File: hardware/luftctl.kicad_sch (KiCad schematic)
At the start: 39 parts, among them J1 PJ-102A, J2 TTL, M1 PWM Fan, M2 PWM Fan, M3 PWM Fan, M4 PWM Fan, M5 PWM Fan, M6 PWM Fan, U1 ESP32-DEVKITC-32D, U2 R-78E5.0-1.0, U3 SN74HCT245N, U5 DS18B20, U6 DS18B20, U7 DS18B20

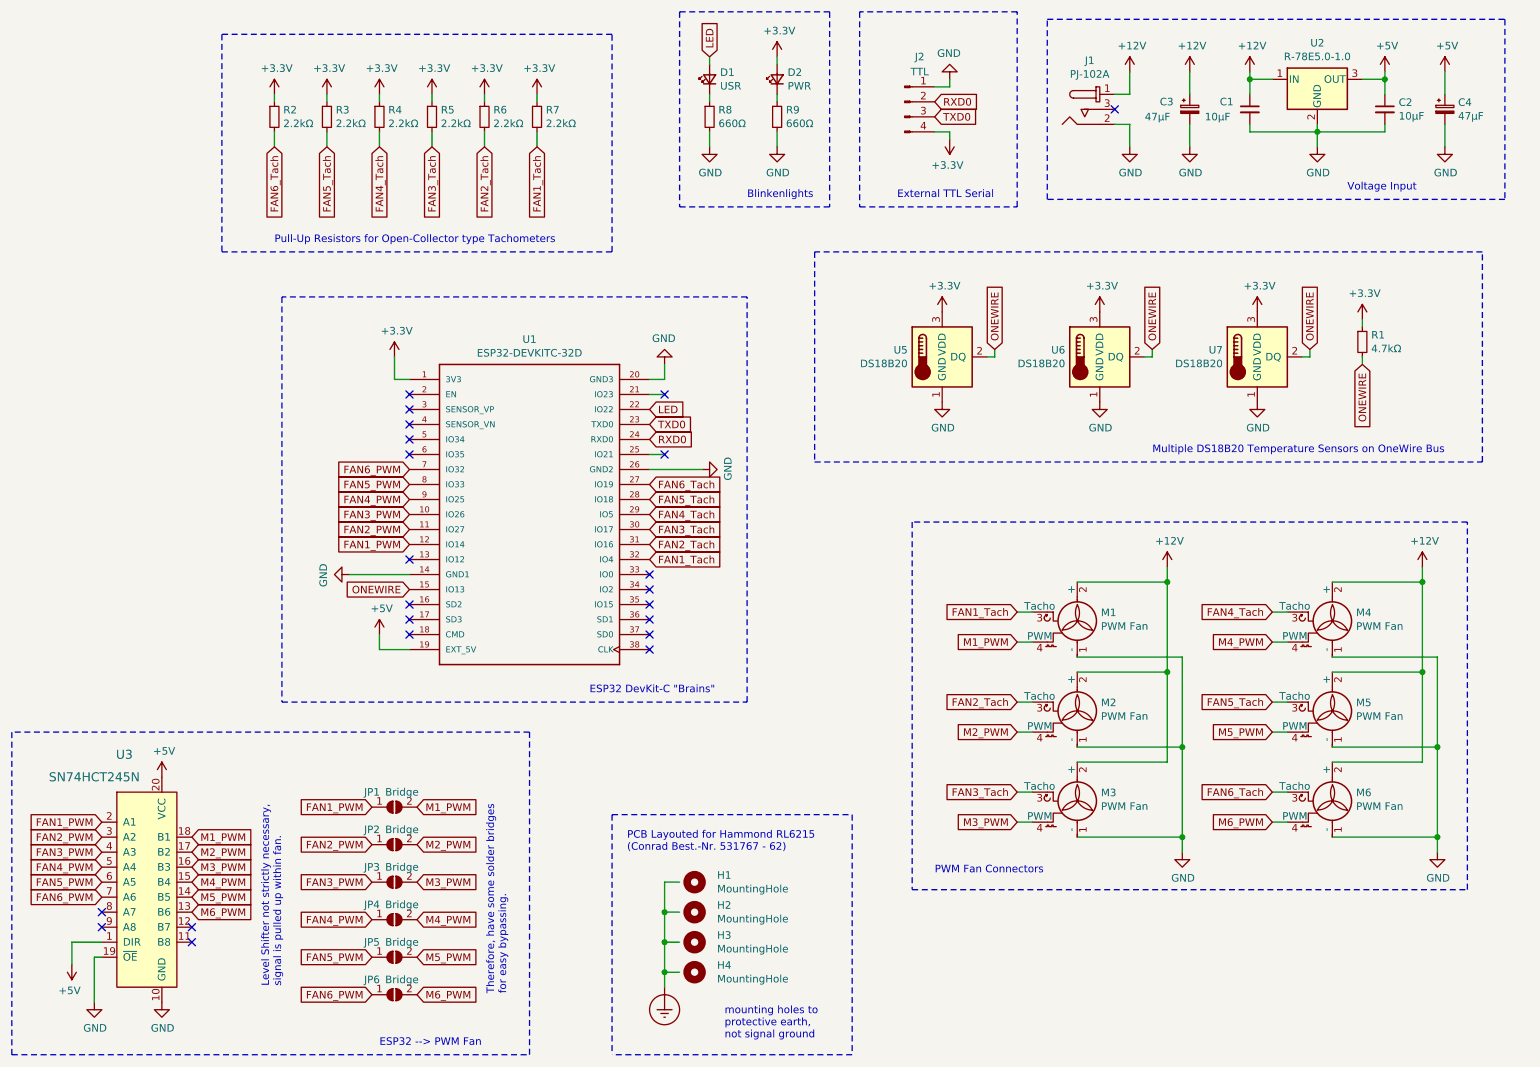
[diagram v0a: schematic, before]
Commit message: redesigned schematic for esp32-c3 module, dummy pcb
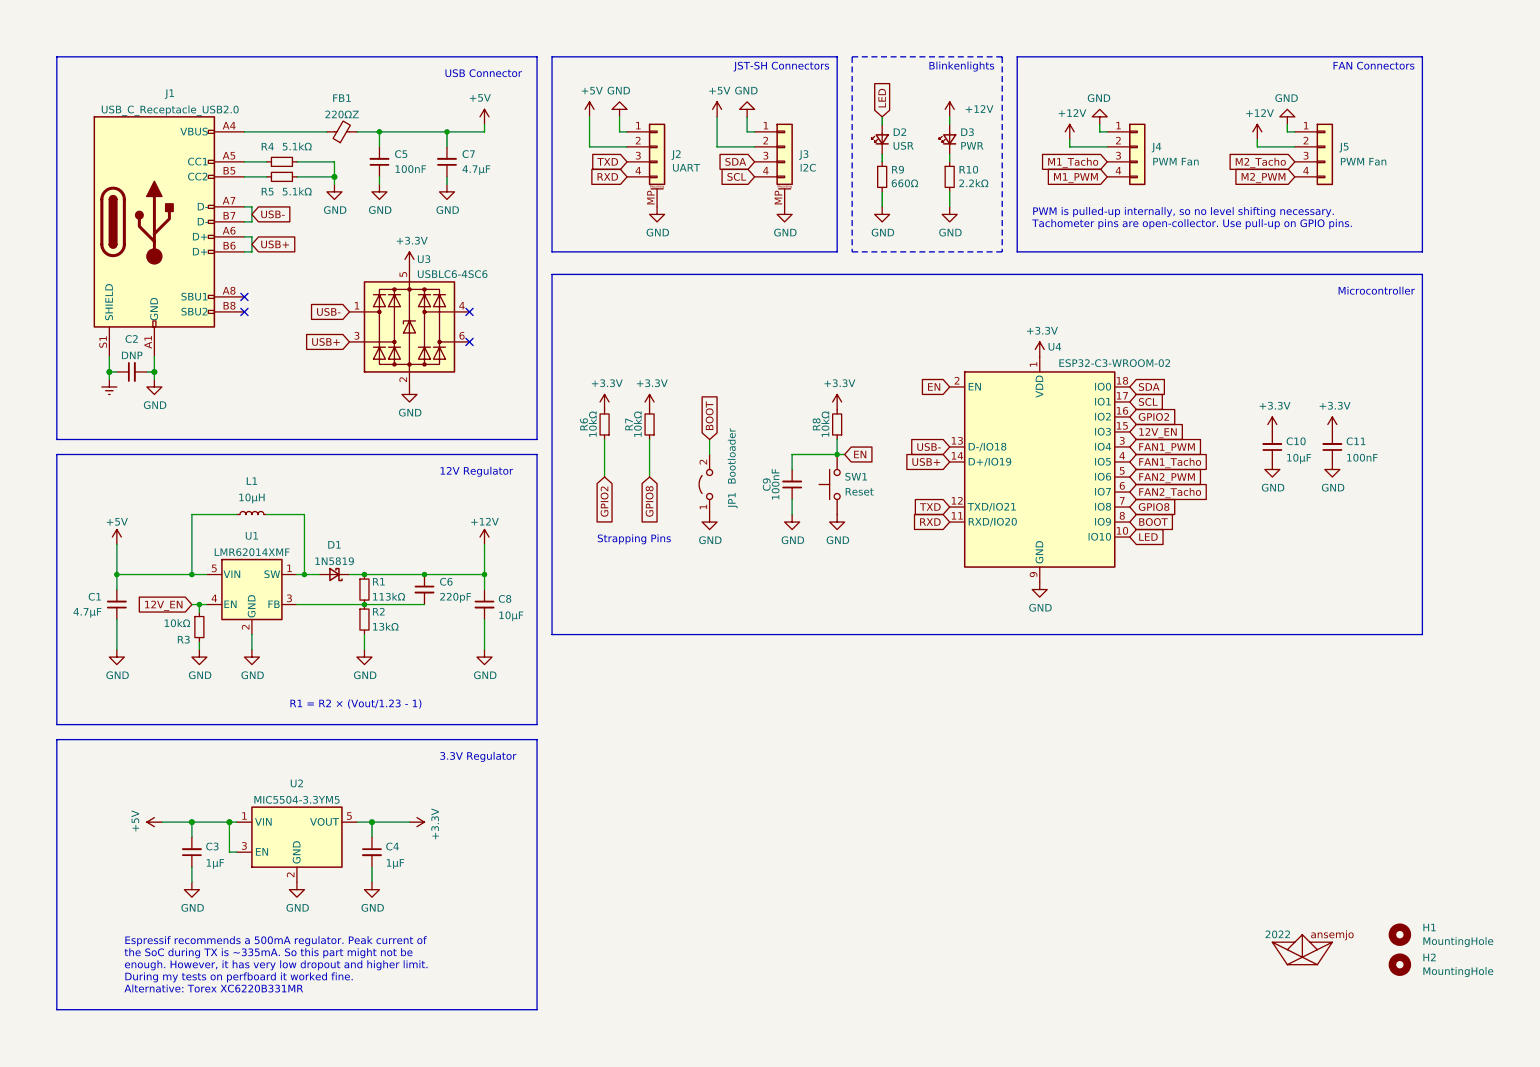
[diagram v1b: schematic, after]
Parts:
- removed C3, C4: 47µF, Capacitor_THT:CP_Radial_D6.3mm_P2.50mm, symbol Device:CP_Small
- removed H3, H4: MountingHole, MountingHole:MountingHole_3.2mm_M3, symbol Mechanical:MountingHole
- removed J1: PJ-102A, digikey-footprints:Barrel_Jack_5.5mmODx2.1mmID_PJ-102A, symbol dk_Barrel-Power-Connectors:PJ-102A
- removed J2: TTL, Connector_PinHeader_2.54mm:PinHeader_1x04_P2.54mm_Vertical, symbol Connector:Conn_01x04_Male
- removed JP1, JP2, JP3, JP4, JP5, JP6: Bridge, Jumper:SolderJumper-2_P1.3mm_Open_TrianglePad1.0x1.5mm, symbol Jumper:SolderJumper_2_Open
- removed M1, M2, M3, M4, M5, M6: PWM Fan, Connector:FanPinHeader_1x04_P2.54mm_Vertical, symbol Motor:Fan_Tacho_PWM
- removed U1: ESP32-DEVKITC-32D, snapeda-lib:MODULE_ESP32-DEVKITC-32D, symbol luftctl-rescue:ESP32-DEVKITC-32D-esp32-devkit
- removed U2: R-78E5.0-1.0, Converter_DCDC:Converter_DCDC_RECOM_R-78E-0.5_THT, symbol Regulator_Switching:R-78E5.0-1.0
- removed U3: SN74HCT245N, Package_DIP:DIP-20_W7.62mm, symbol dk_Logic-Buffers-Drivers-Receivers-Transceivers:SN74LVC245AN
- removed U5, U6, U7: DS18B20, Package_TO_SOT_THT:TO-92_Inline_Wide, symbol Sensor_Temperature:DS18B20
- added A1: 2022, ansemjo:ahoi, symbol ansemjo:ahoi
- added C10, C8: 10µF, Capacitor_SMD:C_0805_2012Metric_Pad1.18x1.45mm_HandSolder, symbol Device:C_Small
- added C11, C5, C9: 100nF, Capacitor_SMD:C_0805_2012Metric_Pad1.18x1.45mm_HandSolder, symbol Device:C_Small
- added C3, C4: 1µF, Capacitor_SMD:C_0805_2012Metric_Pad1.18x1.45mm_HandSolder, symbol Device:C_Small
- added C6: 220pF, Capacitor_SMD:C_0805_2012Metric_Pad1.18x1.45mm_HandSolder, symbol Device:C_Small
- added C7: 4.7µF, Capacitor_SMD:C_0805_2012Metric_Pad1.18x1.45mm_HandSolder, symbol Device:C_Small
- added D1: 1N5819, Diode_SMD:D_SOD-123, symbol Device:D_Schottky_Small
- added FB1: 220ΩZ, Inductor_SMD:L_0805_2012Metric_Pad1.15x1.40mm_HandSolder, symbol Device:Ferrite_Bead_Small
- added J1: USB_C_Receptacle_USB2.0, Connector_USB:USB_C_Receptacle_HRO_TYPE-C-31-M-12, symbol Connector:USB_C_Receptacle_USB2.0
- added J2: UART, Connector_JST:JST_SH_SM04B-SRSS-TB_1x04-1MP_P1.00mm_Horizontal, symbol Connector_Generic_MountingPin:Conn_01x04_MountingPin
- added J3: I2C, Connector_JST:JST_SH_SM04B-SRSS-TB_1x04-1MP_P1.00mm_Horizontal, symbol Connector_Generic_MountingPin:Conn_01x04_MountingPin
- added J4, J5: PWM Fan, Connector:FanPinHeader_1x04_P2.54mm_Vertical, symbol Connector_Generic:Conn_01x04
- added JP1: Bootloader, Button_Switch_SMD:SW_SPST_PTS810, symbol Jumper:Jumper_2_Open
- added L1: 10µH, Inductor_SMD:L_Bourns_SRN6045TA, symbol Device:L_Small
- added R8: 10kΩ, Resistor_SMD:R_0805_2012Metric_Pad1.20x1.40mm_HandSolder, symbol Device:R_Small
- added SW1: Reset, Button_Switch_SMD:SW_SPST_PTS810, symbol Switch:SW_Push
- added U1: LMR62014XMF, Package_TO_SOT_SMD:SOT-23-5, symbol Regulator_Switching:LMR62014XMF
- added U2: MIC5504-3.3YM5, Package_TO_SOT_SMD:SOT-23-5, symbol Regulator_Linear:MIC5504-3.3YM5
- added U3: USBLC6-4SC6, Package_TO_SOT_SMD:SOT-23-6, symbol Power_Protection:USBLC6-4SC6
- added U4: ESP32-C3-WROOM-02, RF_Module:ESP-WROOM-02, symbol local:ESP32-C3-WROOM-02
- C1: value 10µF -> 4.7µF; footprint Capacitor_THT:C_Disc_D5.1mm_W3.2mm_P5.00mm -> Capacitor_SMD:C_0805_2012Metric_Pad1.18x1.45mm_HandSolder
- C2: value 10µF -> DNP; footprint Capacitor_THT:C_Disc_D5.1mm_W3.2mm_P5.00mm -> Capacitor_SMD:C_0805_2012Metric_Pad1.18x1.45mm_HandSolder
- D2: renamed from D1; footprint LED_THT:LED_Rectangular_W5.0mm_H2.0mm -> LED_SMD:LED_0805_2012Metric_Pad1.15x1.40mm_HandSolder
- D3: renamed from D2; footprint LED_THT:LED_Rectangular_W5.0mm_H2.0mm -> LED_SMD:LED_0805_2012Metric_Pad1.15x1.40mm_HandSolder
- H1, H2: footprint MountingHole:MountingHole_3.2mm_M3 -> MountingHole:MountingHole_5.3mm_M5
- R1: value 4.7kΩ -> 113kΩ; footprint Resistor_THT:R_Axial_DIN0207_L6.3mm_D2.5mm_P10.16mm_Horizontal -> Resistor_SMD:R_0805_2012Metric_Pad1.20x1.40mm_HandSolder
- R10: renamed from R9; value 660Ω -> 2.2kΩ; footprint Resistor_THT:R_Axial_DIN0207_L6.3mm_D2.5mm_P10.16mm_Horizontal -> Resistor_SMD:R_0805_2012Metric_Pad1.20x1.40mm_HandSolder
- R2: value 2.2kΩ -> 13kΩ; footprint Resistor_THT:R_Axial_DIN0207_L6.3mm_D2.5mm_P10.16mm_Horizontal -> Resistor_SMD:R_0805_2012Metric_Pad1.20x1.40mm_HandSolder
- R3, R6, R7: value 2.2kΩ -> 10kΩ; footprint Resistor_THT:R_Axial_DIN0207_L6.3mm_D2.5mm_P10.16mm_Horizontal -> Resistor_SMD:R_0805_2012Metric_Pad1.20x1.40mm_HandSolder
- R4, R5: value 2.2kΩ -> 5.1kΩ; footprint Resistor_THT:R_Axial_DIN0207_L6.3mm_D2.5mm_P10.16mm_Horizontal -> Resistor_SMD:R_0805_2012Metric_Pad1.20x1.40mm_HandSolder
- R9: renamed from R8; footprint Resistor_THT:R_Axial_DIN0207_L6.3mm_D2.5mm_P10.16mm_Horizontal -> Resistor_SMD:R_0805_2012Metric_Pad1.20x1.40mm_HandSolder
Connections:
- net FAN1_Tach is gone; now on net +3V3: R7.2
- net FAN2_Tach is gone; now on net +3V3: R6.2
- net FAN4_Tach is gone; now on net GND: R4.2
- net FAN5_Tach is gone; now on net GND: R3.2
- net FAN6_Tach is gone; now on net GND: R2.2
- net +12V: now also D3.2 (A), R1.1, C6.1, C8.1, D1.1 (K), J4.2 (Pin_2), J5.2 (Pin_2); no longer C1.1
- net +3V3: now also C10.2, C11.2, C4.1, R8.2, U2.5 (VOUT), U3.5 (VBUS), U4.1 (VDD); no longer D3.2 (A), R1.1, R2.1, R3.1, R4.1, R5.1, R6.1, R7.1
- net +5V: now also C1.2, C3.2, C5.2, C7.2, FB1.2, J2.2 (Pin_2), J3.2 (Pin_2), L1.1, U1.5 (VIN), U2.1 (VIN), U2.3 (EN); no longer C2.1
- net FAN1_PWM: now also U4.3 (IO4)
- net FAN2_PWM: now also U4.5 (IO6)
- net GND: now also C1.1, R5.1, C10.1, C11.1, C3.1, C4.2, C5.1, C7.1, C8.2, C9.1, J1.A1 (GND), J1.A12 (GND), J1.B1 (GND), J1.B12 (GND), J2.1 (Pin_1), J2.MP (MountPin), J3.1 (Pin_1), J3.MP (MountPin), J4.1 (Pin_1), J5.1 (Pin_1), JP1.1 (A), SW1.1, U1.2 (GND), U2.2 (GND), U3.2 (GND), U4.19 (GND), U4.9 (GND); no longer C1.2
- net LED: now also U4.10 (IO10)
- net M1_PWM: now also J4.4 (Pin_4)
- net M2_PWM: now also J5.4 (Pin_4)
- net FAN3_Tach: no longer names the net of R5.2
- net FAN3_Tach: now also J1.B5 (CC2)
- net ONEWIRE: no longer names the net of R1.2
- net ONEWIRE: now also R2.1, C6.2, U1.3 (FB)
- new net: J1.A5 (CC1), R4.1
- new net: FB1.1, J1.A4 (VBUS), J1.A9 (VBUS), J1.B4 (VBUS), J1.B9 (VBUS)
- new net: D1.2 (A), L1.2, U1.1 (SW)
- new net 12V_EN: R3.1, U1.4 (EN), U4.15 (IO3)
- new net BOOT: JP1.2 (B), U4.8 (IO9)
- new net EN: C9.2, R8.1, SW1.2, U4.2 (EN)
- new net Earth: C2.1, J1.S1 (SHIELD)
- new net FAN1_Tacho: U4.4 (IO5)
- new net FAN2_Tacho: U4.6 (IO7)
- new net GPIO2: R6.1, U4.16 (IO2)
- new net GPIO8: R7.1, U4.7 (IO8)
- new net M1_Tacho: J4.3 (Pin_3)
- new net M2_Tacho: J5.3 (Pin_3)
- new net RXD: J2.4 (Pin_4), U4.11 (RXD/IO20)
- new net SCL: J3.4 (Pin_4), U4.17 (IO1)
- new net SDA: J3.3 (Pin_3), U4.18 (IO0)
- new net TXD: J2.3 (Pin_3), U4.12 (TXD/IO21)
- new net USB+: J1.A6 (D+), J1.B6 (D+), U3.3 (I/O2), U4.14 (D+/IO19)
- new net USB-: J1.A7 (D-), J1.B7 (D-), U3.1 (I/O1), U4.13 (D-/IO18)
- no-connect marks 22 -> 4
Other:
- note added: "12V Regulator"
- note added: "3.3V Regulator"
- note added: "Espressif recommends a 500mA regulator. Peak current of the SoC during TX is ~335mA. So this part might not be enough. However, it has very low dropout and higher limit. During my tests on perfboard it worked fine. Alternative: Torex XC6220B331MR"
- note added: "FAN Connectors"
- note added: "JST-SH Connectors"
- note added: "Microcontroller"
- note added: "PWM is pulled-up internally, so no level shifting necessary. Tachometer pins are open-collector. Use pull-up on GPIO pins."
- note added: "R1 = R2 × (Vout/1.23 - 1)"
- note added: "Strapping Pins"
- note added: "USB Connector"
- note removed: "ESP32 --> PWM Fan"
- note removed: "ESP32 DevKit-C "Brains""
- note removed: "External TTL Serial"
- note removed: "Level Shifter not strictly necessary, signal is pulled up within fan."
- note removed: "Multiple DS18B20 Temperature Sensors on OneWire Bus"
- note removed: "PCB Layouted for Hammond RL6215 (Conrad Best.-Nr. 531767 - 62)"
- note removed: "PWM Fan Connectors"
- note removed: "Pull-Up Resistors for Open-Collector type Tachometers"
- note removed: "Therefore, have some solder bridges for easy bypassing."
- note removed: "Voltage Input"
- note removed: "mounting holes to protective earth, not signal ground"
- moved on the sheet: D2, D3, H1, H2, R10, R9

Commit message: finished pcb layout
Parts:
- removed C2: DNP, Capacitor_SMD:C_0805_2012Metric_Pad1.18x1.45mm_HandSolder, symbol Device:C_Small
- removed H1, H2: MountingHole, MountingHole:MountingHole_5.3mm_M5, symbol Mechanical:MountingHole
- added TP1, TP2, TP3, TP4: Test, TestPoint:TestPoint_THTPad_D1.5mm_Drill0.7mm, symbol Connector:TestPoint_Probe
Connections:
- net Earth is gone; now on net GND: J1.S1 (SHIELD)
- net M1_PWM is gone; now on net FAN1_PWM: J4.4 (Pin_4)
- net M1_Tacho is gone; now on net FAN1_Tacho: J4.3 (Pin_3)
- net M2_PWM is gone; now on net FAN2_PWM: J5.4 (Pin_4)
- net M2_Tacho is gone; now on net FAN2_Tacho: J5.3 (Pin_3)
- net +12V: now also TP1.1
- net +3V3: now also TP3.1; no longer U3.5 (VBUS)
- net +5V: now also TP2.1
- net GND: now also TP4.1
- net USB-: now also U3.4 (I/O3); no longer U3.1 (I/O1)
- net CC2: now reaches J1.B5 (CC2), R5.2
- net CC2: now also U3.1 (I/O1)
- net CC1: now reaches J1.A5 (CC1), R4.1
- net CC1: now also U3.6 (I/O4)
- net VBUS: now reaches FB1.1, J1.A4 (VBUS), J1.A9 (VBUS), J1.B4 (VBUS), J1.B9 (VBUS)
- net VBUS: now also U3.5 (VBUS)
- no-connect marks 4 -> 2
